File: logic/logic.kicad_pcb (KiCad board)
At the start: 2 copper layers, 33 x 39.5 mm, 5 parts, among them J0 COLS, J1 ROWS, J2 ISP-PROG-6, U0 ATSAMD21G18A-AUT, U1 BMA250E

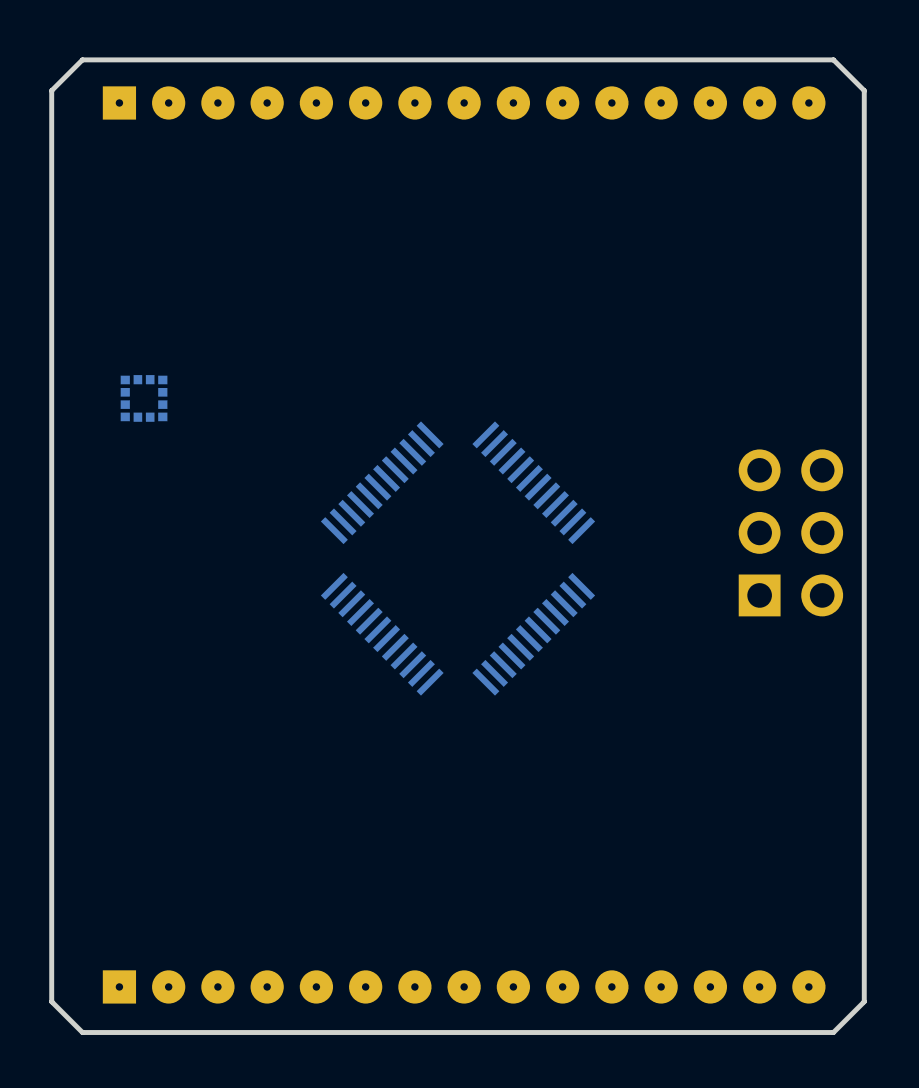
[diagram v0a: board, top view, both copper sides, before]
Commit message: update logic board outline
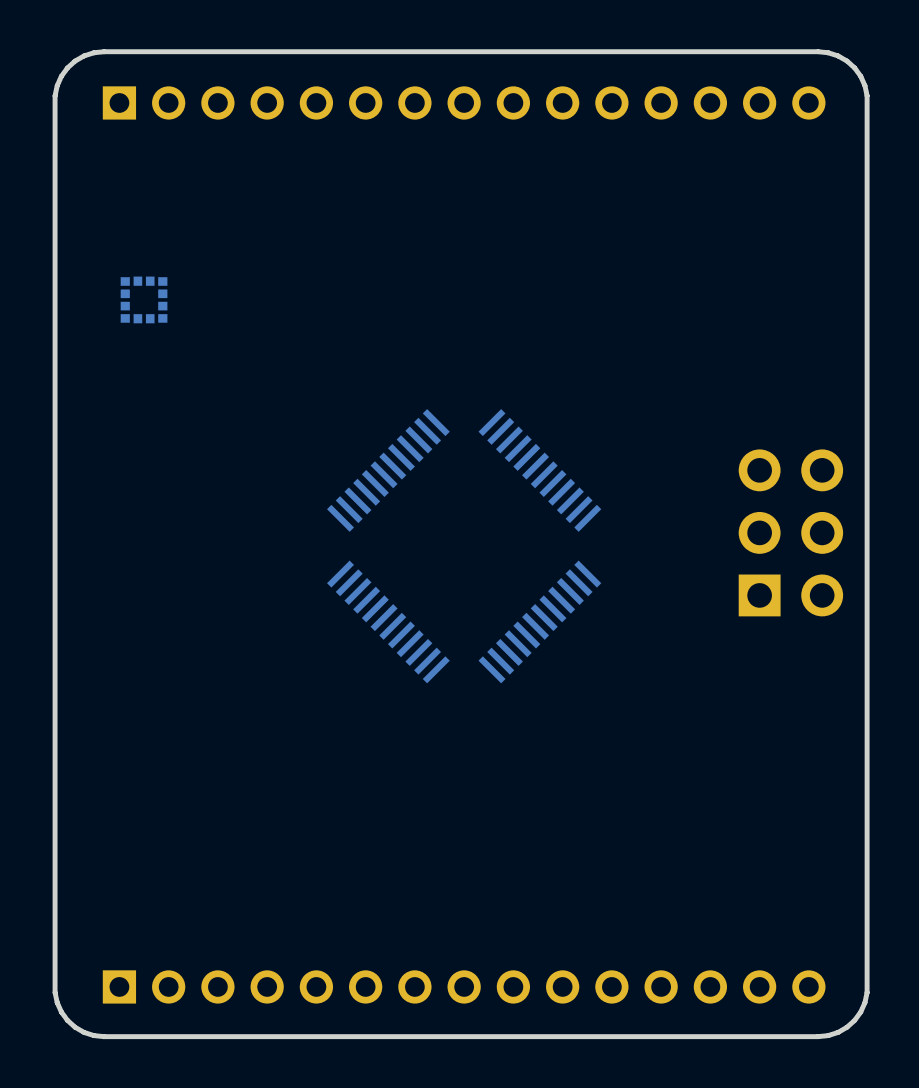
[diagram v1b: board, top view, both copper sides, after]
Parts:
- J2: footprint Pin_Headers:Pin_Header_Straight_2x03_Pitch2.54mm -> Connector_PinHeader_2.54mm:PinHeader_2x03_P2.54mm_Vertical
- U1: footprint Housings_LGA:LGA-12_2x2mm_Pitch0.5mm -> Package_LGA:LGA-12_2x2mm_P0.5mm
- moved U1 4.00 mm to (133.0, 67.0)
- moved U0 0.56 mm to (146.0, 77.0)
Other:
- board size 33 x 39.5 mm -> 33 x 40 mm

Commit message: Reassign pins to avoid crossing
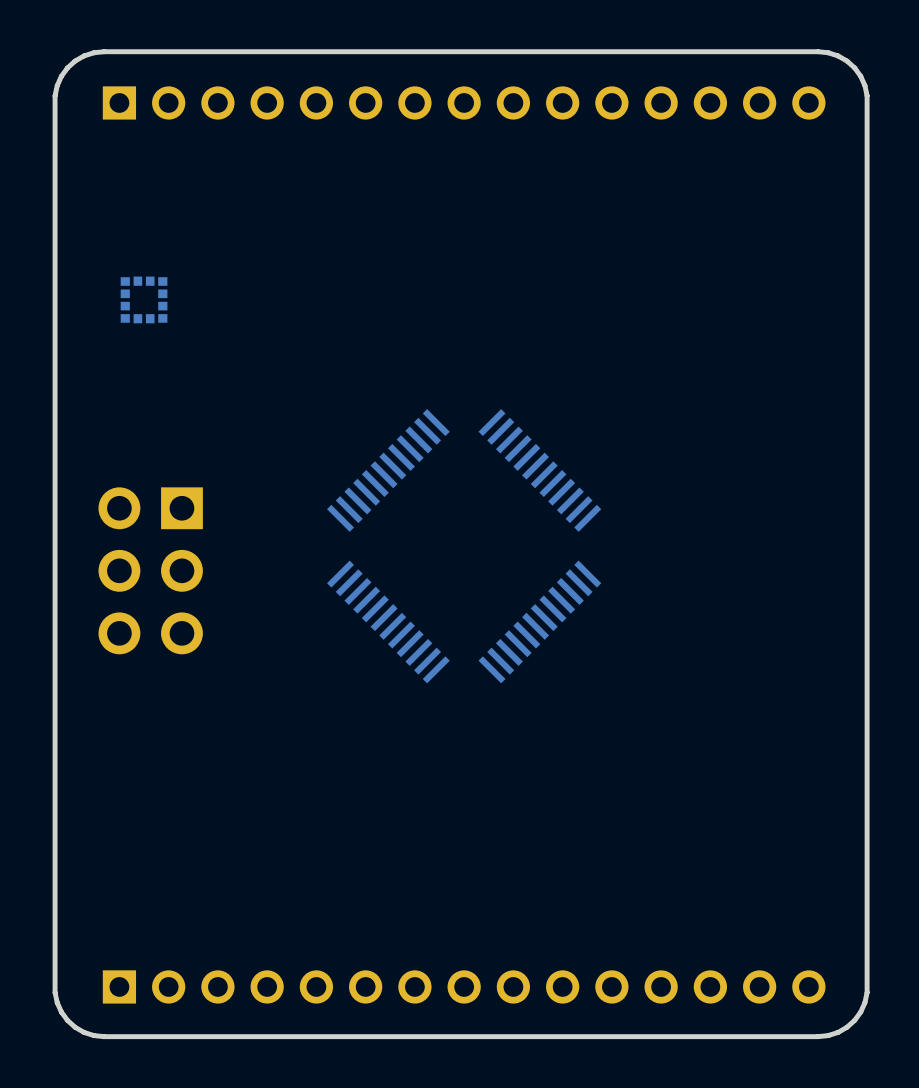
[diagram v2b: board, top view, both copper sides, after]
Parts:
- moved J2 23.7 mm to (134.5, 75.5), turned to 180 degrees
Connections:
- U0 pad 31: ROW_7 -> ROW_14
- U0 pad 32: ROW_8 -> ROW_13
- U0 pad 33: ROW_9 -> ROW_12
- U0 pad 34: ROW_10 -> ROW_11
- U0 pad 37: (no net) -> ROW_10
- U0 pad 38: (no net) -> ROW_9
- U0 pad 39: ROW_11 -> ROW_8
- U0 pad 41: ROW_12 -> ROW_7
- U0 pad 45: ROW_13 -> SWCLK
- U0 pad 46: ROW_14 -> SWDIO
- U0 pad 47: SWCLK -> (no net)
- U0 pad 48: SWDIO -> (no net)
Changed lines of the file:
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@@
     (pad 2 smd rect (at -4.35 2.25 315) (size 1.3 0.25) (layers B.Cu B.Paste B.Mask)
       (net 13 COL_1))
-    (pad 3 smd rect (at -4.35 1.75 315) (size 1.3 0.25) (layers B.Cu B.Paste B.Mask)
+    (pad 3 smd rect (at -4.35 1.749999 315) (size 1.3 0.25) (layers B.Cu B.Paste B.Mask)
       (net 14 COL_2))
     (pad 4 smd rect (at -4.35 1.25 315) (size 1.3 0.25) (layers B.Cu B.Paste B.Mask)
       (net 15 COL_3))
-    (pad 5 smd rect (at -4.35 0.75 315) (size 1.3 0.25) (layers B.Cu B.Paste B.Mask))
+    (pad 5 smd rect (at -4.35 0.750001 315) (size 1.3 0.25) (layers B.Cu B.Paste B.Mask))
     (pad 6 smd rect (at -4.35 0.25 315) (size 1.3 0.25) (layers B.Cu B.Paste B.Mask))
     (pad 7 smd rect (at -4.35 -0.25 315) (size 1.3 0.25) (layers B.Cu B.Paste B.Mask))
-    (pad 8 smd rect (at -4.35 -0.75 315) (size 1.3 0.25) (layers B.Cu B.Paste B.Mask))
+    (pad 8 smd rect (at -4.35 -0.750001 315) (size 1.3 0.25) (layers B.Cu B.Paste B.Mask))
     (pad 9 smd rect (at -4.35 -1.25 315) (size 1.3 0.25) (layers B.Cu B.Paste B.Mask)
       (net 16 COL_4))
-    (pad 10 smd rect (at -4.35 -1.75 315) (size 1.3 0.25) (layers B.Cu B.Paste B.Mask)
+    (pad 10 smd rect (at -4.35 -1.749999 315) (size 1.3 0.25) (layers B.Cu B.Paste B.Mask)
       (net 17 COL_5))
     (pad 11 smd rect (at -4.35 -2.25 315) (size 1.3 0.25) (layers B.Cu B.Paste B.Mask)
@@
     (pad 14 smd rect (at -2.25 -4.35 225) (size 1.3 0.25) (layers B.Cu B.Paste B.Mask)
       (net 21 COL_9))
-    (pad 15 smd rect (at -1.75 -4.35 225) (size 1.3 0.25) (layers B.Cu B.Paste B.Mask)
+    (pad 15 smd rect (at -1.749999 -4.35 225) (size 1.3 0.25) (layers B.Cu B.Paste B.Mask)
       (net 22 COL_10))
     (pad 16 smd rect (at -1.25 -4.35 225) (size 1.3 0.25) (layers B.Cu B.Paste B.Mask)
       (net 23 COL_11))
-    (pad 17 smd rect (at -0.75 -4.35 225) (size 1.3 0.25) (layers B.Cu B.Paste B.Mask)
+    (pad 17 smd rect (at -0.750001 -4.35 225) (size 1.3 0.25) (layers B.Cu B.Paste B.Mask)
       (net 31 "Net-(U0-Pad17)"))
     (pad 18 smd rect (at -0.25 -4.35 225) (size 1.3 0.25) (layers B.Cu B.Paste B.Mask)
       (net 32 "Net-(U0-Pad18)"))
     (pad 19 smd rect (at 0.25 -4.35 225) (size 1.3 0.25) (layers B.Cu B.Paste B.Mask))
-    (pad 20 smd rect (at 0.75 -4.35 225) (size 1.3 0.25) (layers B.Cu B.Paste B.Mask))
+    (pad 20 smd rect (at 0.750001 -4.35 225) (size 1.3 0.25) (layers B.Cu B.Paste B.Mask))
     (pad 21 smd rect (at 1.25 -4.35 225) (size 1.3 0.25) (layers B.Cu B.Paste B.Mask)
       (net 24 COL_12))
-    (pad 22 smd rect (at 1.75 -4.35 225) (size 1.3 0.25) (layers B.Cu B.Paste B.Mask)
+    (pad 22 smd rect (at 1.749999 -4.35 225) (size 1.3 0.25) (layers B.Cu B.Paste B.Mask)
       (net 25 COL_13))
     (pad 23 smd rect (at 2.25 -4.35 225) (size 1.3 0.25) (layers B.Cu B.Paste B.Mask)
@@
     (pad 26 smd rect (at 4.35 -2.25 315) (size 1.3 0.25) (layers B.Cu B.Paste B.Mask)
       (net 3 ROW_2))
-    (pad 27 smd rect (at 4.35 -1.75 315) (size 1.3 0.25) (layers B.Cu B.Paste B.Mask)
+    (pad 27 smd rect (at 4.35 -1.749999 315) (size 1.3 0.25) (layers B.Cu B.Paste B.Mask)
       (net 4 ROW_3))
     (pad 28 smd rect (at 4.35 -1.25 315) (size 1.3 0.25) (layers B.Cu B.Paste B.Mask)
       (net 5 ROW_4))
-    (pad 29 smd rect (at 4.35 -0.75 315) (size 1.3 0.25) (layers B.Cu B.Paste B.Mask)
+    (pad 29 smd rect (at 4.35 -0.750001 315) (size 1.3 0.25) (layers B.Cu B.Paste B.Mask)
       (net 6 ROW_5))
     (pad 30 smd rect (at 4.35 -0.25 315) (size 1.3 0.25) (layers B.Cu B.Paste B.Mask)
       (net 7 ROW_6))
     (pad 31 smd rect (at 4.35 0.25 315) (size 1.3 0.25) (layers B.Cu B.Paste B.Mask)
-      (net 8 ROW_7))
-    (pad 32 smd rect (at 4.35 0.75 315) (size 1.3 0.25) (layers B.Cu B.Paste B.Mask)
-      (net 9 ROW_8))
+      (net 30 ROW_14))
+    (pad 32 smd rect (at 4.35 0.750001 315) (size 1.3 0.25) (layers B.Cu B.Paste B.Mask)
+      (net 29 ROW_13))
     (pad 33 smd rect (at 4.35 1.25 315) (size 1.3 0.25) (layers B.Cu B.Paste B.Mask)
-      (net 10 ROW_9))
-    (pad 34 smd rect (at 4.35 1.75 315) (size 1.3 0.25) (layers B.Cu B.Paste B.Mask)
-      (net 11 ROW_10))
+      (net 28 ROW_12))
+    (pad 34 smd rect (at 4.35 1.749999 315) (size 1.3 0.25) (layers B.Cu B.Paste B.Mask)
+      (net 27 ROW_11))
     (pad 35 smd rect (at 4.35 2.25 315) (size 1.3 0.25) (layers B.Cu B.Paste B.Mask)
       (net 32 "Net-(U0-Pad18)"))
     (pad 36 smd rect (at 4.35 2.75 315) (size 1.3 0.25) (layers B.Cu B.Paste B.Mask)
       (net 31 "Net-(U0-Pad17)"))
-    (pad 37 smd rect (at 2.75 4.35 225) (size 1.3 0.25) (layers B.Cu B.Paste B.Mask))
-    (pad 38 smd rect (at 2.25 4.35 225) (size 1.3 0.25) (layers B.Cu B.Paste B.Mask))
-    (pad 39 smd rect (at 1.75 4.35 225) (size 1.3 0.25) (layers B.Cu B.Paste B.Mask)
-      (net 27 ROW_11))
+    (pad 37 smd rect (at 2.75 4.35 225) (size 1.3 0.25) (layers B.Cu B.Paste B.Mask)
+      (net 11 ROW_10))
+    (pad 38 smd rect (at 2.25 4.35 225) (size 1.3 0.25) (layers B.Cu B.Paste B.Mask)
+      (net 10 ROW_9))
+    (pad 39 smd rect (at 1.749999 4.35 225) (size 1.3 0.25) (layers B.Cu B.Paste B.Mask)
+      (net 9 ROW_8))
     (pad 40 smd rect (at 1.25 4.35 225) (size 1.3 0.25) (layers B.Cu B.Paste B.Mask)
       (net 33 RESET))
-    (pad 41 smd rect (at 0.75 4.35 225) (size 1.3 0.25) (layers B.Cu B.Paste B.Mask)
-      (net 28 ROW_12))
+    (pad 41 smd rect (at 0.750001 4.35 225) (size 1.3 0.25) (layers B.Cu B.Paste B.Mask)
+      (net 8 ROW_7))
     (pad 42 smd rect (at 0.25 4.35 225) (size 1.3 0.25) (layers B.Cu B.Paste B.Mask)
       (net 32 "Net-(U0-Pad18)"))
     (pad 43 smd rect (at -0.25 4.35 225) (size 1.3 0.25) (layers B.Cu B.Paste B.Mask))
-    (pad 44 smd rect (at -0.75 4.35 225) (size 1.3 0.25) (layers B.Cu B.Paste B.Mask))
+    (pad 44 smd rect (at -0.750001 4.35 225) (size 1.3 0.25) (layers B.Cu B.Paste B.Mask))
     (pad 45 smd rect (at -1.25 4.35 225) (size 1.3 0.25) (layers B.Cu B.Paste B.Mask)
-      (net 29 ROW_13))
-    (pad 46 smd rect (at -1.75 4.35 225) (size 1.3 0.25) (layers B.Cu B.Paste B.Mask)
-      (net 30 ROW_14))
-    (pad 47 smd rect (at -2.25 4.35 225) (size 1.3 0.25) (layers B.Cu B.Paste B.Mask)
       (net 34 SWCLK))
-    (pad 48 smd rect (at -2.75 4.35 225) (size 1.3 0.25) (layers B.Cu B.Paste B.Mask)
+    (pad 46 smd rect (at -1.749999 4.35 225) (size 1.3 0.25) (layers B.Cu B.Paste B.Mask)
       (net 35 SWDIO))
+    (pad 47 smd rect (at -2.25 4.35 225) (size 1.3 0.25) (layers B.Cu B.Paste B.Mask))
+    (pad 48 smd rect (at -2.75 4.35 225) (size 1.3 0.25) (layers B.Cu B.Paste B.Mask))
     (model ${KISYS3DMOD}/Package_QFP.3dshapes/TQFP-48_7x7mm_P0.5mm.wrl
       (at (xyz 0 0 0))
@@
   )
   (module Connector_PinHeader_2.54mm:PinHeader_2x03_P2.54mm_Vertical (layer B.Cu)
-    (at 158 79)
+    (at 134.54 75.46 180)
     (descr "Through hole straight pin header, 2x03, 2.54mm pitch, double rows")
     (tags "Through hole pin header THT 2x03 2.54mm double row")
-    (fp_text reference J2 (at 1.27 2.33) (layer B.SilkS)
+    (fp_text reference J2 (at 1.27 2.33 180) (layer B.SilkS)
       (effects (font (size 1 1) (thickness 0.15)) (justify mirror))
     )
-    (fp_text value ISP-PROG-6 (at 1.27 -7.41) (layer B.Fab)
+    (fp_text value ISP-PROG-6 (at 1.27 -7.41 180) (layer B.Fab)
       (effects (font (size 1 1) (thickness 0.15)) (justify mirror))
     )
@@
     (fp_line (start 4.35 -6.85) (end 4.35 1.8) (layer B.CrtYd) (width 0.05))
     (fp_line (start 4.35 1.8) (end -1.8 1.8) (layer B.CrtYd) (width 0.05))
-    (fp_text user %R (at 1.27 -2.54 -90) (layer B.Fab)
+    (fp_text user %R (at 1.27 -2.54 90) (layer B.Fab)
       (effects (font (size 1 1) (thickness 0.15)) (justify mirror))
     )
-    (pad 1 thru_hole rect (at 0 0) (size 1.7 1.7) (drill 1) (layers *.Cu *.Mask)
+    (pad 1 thru_hole rect (at 0 0 180) (size 1.7 1.7) (drill 1) (layers *.Cu *.Mask)
       (net 35 SWDIO))
-    (pad 2 thru_hole oval (at 2.54 0) (size 1.7 1.7) (drill 1) (layers *.Cu *.Mask))
-    (pad 3 thru_hole oval (at 0 -2.54) (size 1.7 1.7) (drill 1) (layers *.Cu *.Mask)
+    (pad 2 thru_hole oval (at 2.54 0 180) (size 1.7 1.7) (drill 1) (layers *.Cu *.Mask))
+    (pad 3 thru_hole oval (at 0 -2.54 180) (size 1.7 1.7) (drill 1) (layers *.Cu *.Mask)
       (net 34 SWCLK))
-    (pad 4 thru_hole oval (at 2.54 -2.54) (size 1.7 1.7) (drill 1) (layers *.Cu *.Mask))
-    (pad 5 thru_hole oval (at 0 -5.08) (size 1.7 1.7) (drill 1) (layers *.Cu *.Mask)
+    (pad 4 thru_hole oval (at 2.54 -2.54 180) (size 1.7 1.7) (drill 1) (layers *.Cu *.Mask))
+    (pad 5 thru_hole oval (at 0 -5.08 180) (size 1.7 1.7) (drill 1) (layers *.Cu *.Mask)
       (net 33 RESET))
-    (pad 6 thru_hole oval (at 2.54 -5.08) (size 1.7 1.7) (drill 1) (layers *.Cu *.Mask))
+    (pad 6 thru_hole oval (at 2.54 -5.08 180) (size 1.7 1.7) (drill 1) (layers *.Cu *.Mask))
     (model ${KISYS3DMOD}/Connector_PinHeader_2.54mm.3dshapes/PinHeader_2x03_P2.54mm_Vertical.wrl
       (at (xyz 0 0 0))

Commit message: Add power net and route matrix connections
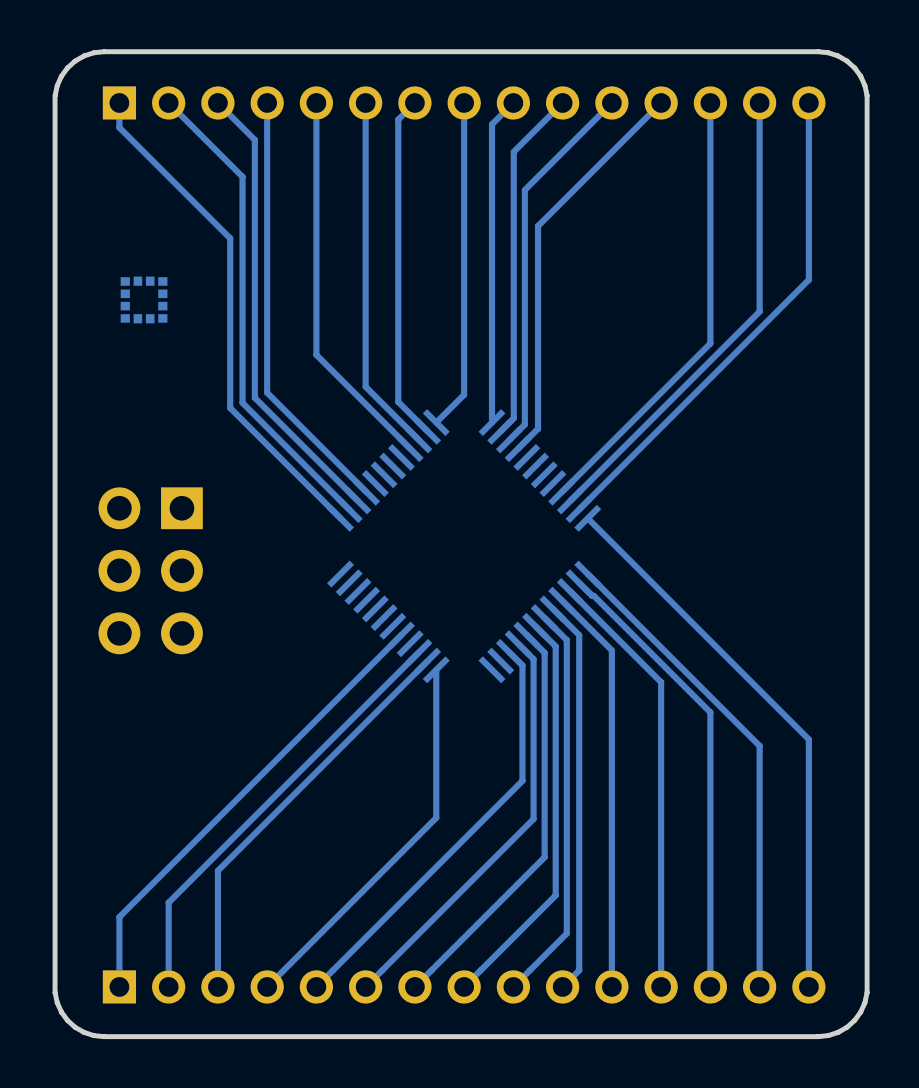
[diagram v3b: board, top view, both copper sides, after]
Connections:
- J2 pad 2: (no net) -> +3V3
- J2 pad 6: (no net) -> GND
- U0 pad 17: Net-(U0-Pad17) -> +3V3
- U0 pad 18: Net-(U0-Pad18) -> GND
- U0 pad 35: Net-(U0-Pad18) -> GND
- U0 pad 36: Net-(U0-Pad17) -> +3V3
- U0 pad 42: Net-(U0-Pad18) -> GND
- U0 pad 43: (no net) -> +3V3
- U0 pad 44: (no net) -> +3V3
- U0 pad 5: (no net) -> GND
- U0 pad 6: (no net) -> +3V3
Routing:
- net ROW_0: track 0.00 -> 22.8 mm
- net COL_0: track 0.00 -> 20.6 mm
- net COL_14: track 0.00 -> 20.4 mm
- net ROW_1: track 0.00 -> 19.7 mm
- net COL_1: track 0.00 -> 19.6 mm
- net COL_13: track 0.00 -> 19.3 mm
- net ROW_7: track 0.00 -> 19.0 mm
- net ROW_2: track 0.00 -> 18.7 mm
- net COL_2: track 0.00 -> 18.5 mm
- net COL_12: track 0.00 -> 18.3 mm
- net ROW_8: track 0.00 -> 17.8 mm
- net ROW_3: track 0.00 -> 17.6 mm
- net COL_3: track 0.00 -> 17.5 mm
- net ROW_11: track 0.00 -> 17.3 mm
- net ROW_12: track 0.00 -> 17.0 mm
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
